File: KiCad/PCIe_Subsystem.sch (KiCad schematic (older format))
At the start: 0 parts

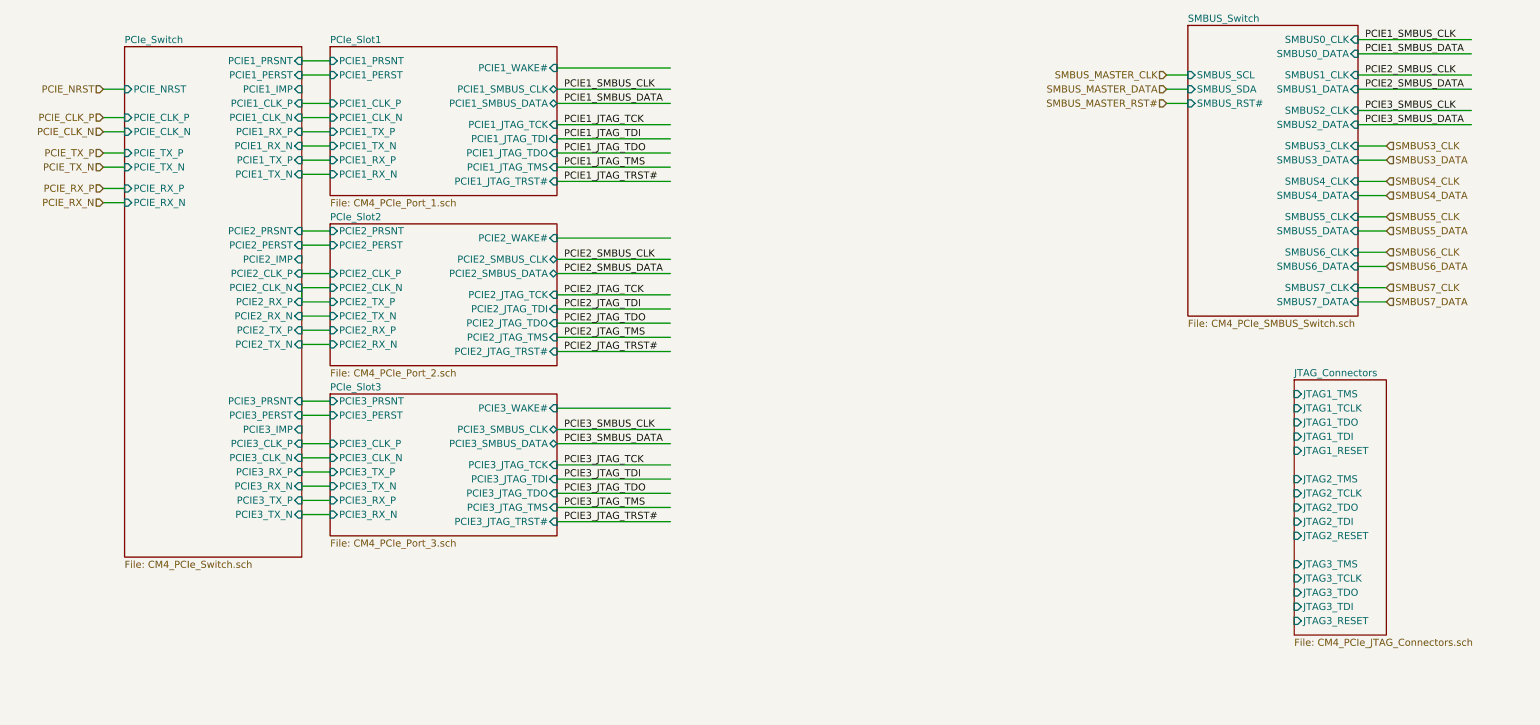
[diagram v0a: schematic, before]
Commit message: Tons of wiring and pin straps for PCI-e Switch
Also re-did some hierarchical labels for JTAG
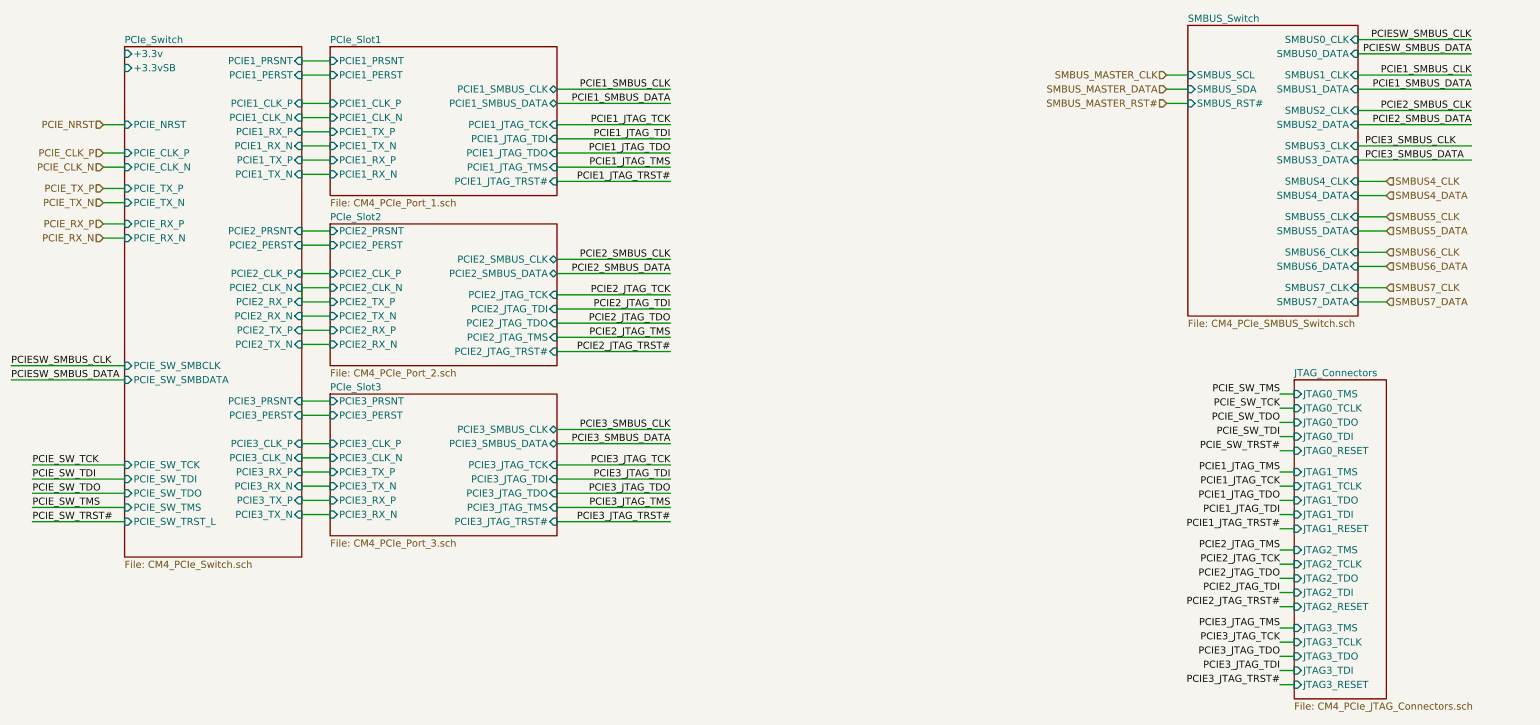
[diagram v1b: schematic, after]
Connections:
- net labels added: PCIESW_SMBUS_CLK, PCIESW_SMBUS_DATA, PCIE_SW_TCK, PCIE_SW_TDI, PCIE_SW_TDO, PCIE_SW_TMS, PCIE_SW_TRST#
- net labels removed: SMBUS3_CLK, SMBUS3_DATA
- wire segments 75 -> 99

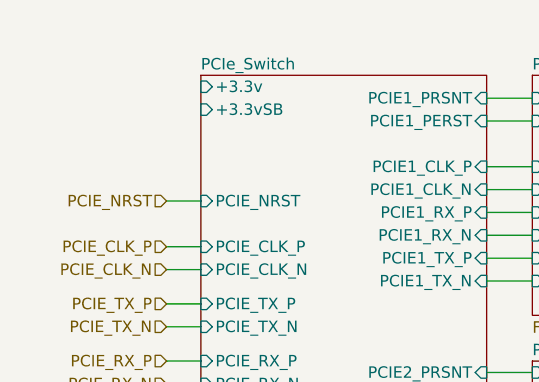
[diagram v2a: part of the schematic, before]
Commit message: PCIe Wiring, resistor value adjustments, and a bunch of small ERC fixes.
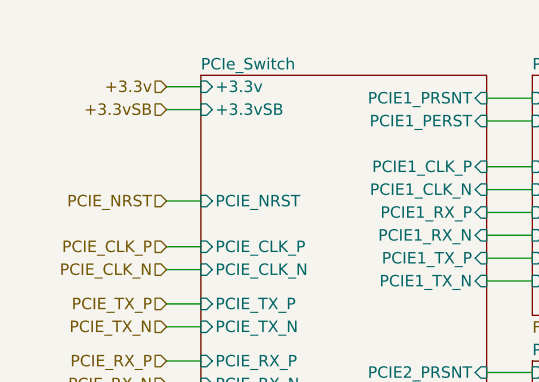
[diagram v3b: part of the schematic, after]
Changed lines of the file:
@@
 Comment4 ""
 $EndDescr
-$Sheet
-S 1300 800  1250 3600
-U 5FFBFEFE
-F0 "PCIe_Switch" 50
-F1 "CM4_PCIe_Switch.sch" 50
-F2 "PCIE_CLK_N" I L 1300 1650 50
-F3 "PCIE_CLK_P" I L 1300 1550 50
-F4 "PCIE_RX_P" I L 1300 2050 50
-F5 "PCIE_RX_N" I L 1300 2150 50
-F6 "PCIE_TX_P" I L 1300 1800 50
-F7 "PCIE_TX_N" I L 1300 1900 50
-F8 "PCIE_NRST" I L 1300 1350 50
-F9 "PCIE1_PRSNT" I R 2550 900 50
-F10 "PCIE2_PRSNT" I R 2550 2100 50
-F11 "PCIE3_PRSNT" I R 2550 3300 50
-F12 "PCIE1_PERST" I R 2550 1000 50
-F13 "PCIE2_PERST" I R 2550 2200 50
-F14 "PCIE3_PERST" I R 2550 3400 50
-F15 "PCIE3_CLK_N" I R 2550 3700 50
-F16 "PCIE3_CLK_P" I R 2550 3600 50
-F17 "PCIE2_CLK_N" I R 2550 2500 50
-F18 "PCIE2_CLK_P" I R 2550 2400 50
-F19 "PCIE1_CLK_N" I R 2550 1300 50
-F20 "PCIE1_CLK_P" I R 2550 1200 50
-F21 "PCIE1_RX_P" I R 2550 1400 50
-F22 "PCIE1_RX_N" I R 2550 1500 50
-F23 "PCIE1_TX_P" I R 2550 1600 50
-F24 "PCIE1_TX_N" I R 2550 1700 50
-F25 "PCIE2_RX_P" I R 2550 2600 50
-F26 "PCIE2_RX_N" I R 2550 2700 50
-F27 "PCIE2_TX_P" I R 2550 2800 50
-F28 "PCIE2_TX_N" I R 2550 2900 50
-F29 "PCIE3_TX_N" I R 2550 4100 50
-F30 "PCIE3_TX_P" I R 2550 4000 50
-F31 "PCIE3_RX_N" I R 2550 3900 50
-F32 "PCIE3_RX_P" I R 2550 3800 50
-F33 "+3.3v" I L 1300 850 50
-F34 "+3.3vSB" I L 1300 950 50
-F35 "PCIE_SW_TDI" I L 1300 3850 50
-F36 "PCIE_SW_TMS" I L 1300 4050 50
-F37 "PCIE_SW_TCK" I L 1300 3750 50
-F38 "PCIE_SW_TDO" I L 1300 3950 50
-F39 "PCIE_SW_TRST_L" I L 1300 4150 50
-F40 "PCIE_SW_SMBCLK" I L 1300 3050 50
-F41 "PCIE_SW_SMBDATA" I L 1300 3150 50
-$EndSheet
 Wire Wire Line
 	2750 4100 2550 4100
@@
 Wire Wire Line
 	2550 900  2750 900
-$Sheet
-S 2750 2050 1600 1000
-U 5FFBFF20
-F0 "PCIe_Slot2" 50
-F1 "CM4_PCIe_Port_2.sch" 50
-F2 "PCIE2_PRSNT" I L 2750 2100 50
-F3 "PCIE2_PERST" I L 2750 2200 50
-F4 "PCIE2_CLK_P" I L 2750 2400 50
-F5 "PCIE2_CLK_N" I L 2750 2500 50
-F6 "PCIE2_RX_P" I L 2750 2800 50
-F7 "PCIE2_RX_N" I L 2750 2900 50
-F8 "PCIE2_TX_N" I L 2750 2700 50
-F9 "PCIE2_TX_P" I L 2750 2600 50
-F10 "PCIE2_SMBUS_CLK" B R 4350 2300 50
-F11 "PCIE2_SMBUS_DATA" B R 4350 2400 50
-F12 "PCIE2_JTAG_TCK" I R 4350 2550 50
-F13 "PCIE2_JTAG_TDI" I R 4350 2650 50
-F14 "PCIE2_JTAG_TDO" I R 4350 2750 50
-F15 "PCIE2_JTAG_TMS" I R 4350 2850 50
-F16 "PCIE2_JTAG_TRST#" I R 4350 2950 50
-$EndSheet
-$Sheet
-S 2750 800  1600 1050
-U 5FFBFF2A
-F0 "PCIe_Slot1" 50
-F1 "CM4_PCIe_Port_1.sch" 50
-F2 "PCIE1_RX_P" I L 2750 1600 50
-F3 "PCIE1_RX_N" I L 2750 1700 50
-F4 "PCIE1_CLK_N" I L 2750 1300 50
-F5 "PCIE1_CLK_P" I L 2750 1200 50
-F6 "PCIE1_PERST" I L 2750 1000 50
-F7 "PCIE1_PRSNT" I L 2750 900 50
-F8 "PCIE1_TX_P" I L 2750 1400 50
-F9 "PCIE1_TX_N" I L 2750 1500 50
-F10 "PCIE1_SMBUS_CLK" B R 4350 1100 50
-F11 "PCIE1_SMBUS_DATA" B R 4350 1200 50
-F12 "PCIE1_JTAG_TCK" I R 4350 1350 50
-F13 "PCIE1_JTAG_TDI" I R 4350 1450 50
-F14 "PCIE1_JTAG_TDO" I R 4350 1550 50
-F15 "PCIE1_JTAG_TMS" I R 4350 1650 50
-F16 "PCIE1_JTAG_TRST#" I R 4350 1750 50
-$EndSheet
-$Sheet
-S 2750 3250 1600 1000
-U 5FFBFF34
-F0 "PCIe_Slot3" 50
-F1 "CM4_PCIe_Port_3.sch" 50
-F2 "PCIE3_PRSNT" I L 2750 3300 50
-F3 "PCIE3_PERST" I L 2750 3400 50
-F4 "PCIE3_CLK_P" I L 2750 3600 50
-F5 "PCIE3_CLK_N" I L 2750 3700 50
-F6 "PCIE3_RX_N" I L 2750 4100 50
-F7 "PCIE3_RX_P" I L 2750 4000 50
-F8 "PCIE3_TX_P" I L 2750 3800 50
-F9 "PCIE3_TX_N" I L 2750 3900 50
-F10 "PCIE3_SMBUS_CLK" B R 4350 3500 50
-F11 "PCIE3_SMBUS_DATA" B R 4350 3600 50
-F12 "PCIE3_JTAG_TCK" I R 4350 3750 50
-F13 "PCIE3_JTAG_TDI" I R 4350 3850 50
-F14 "PCIE3_JTAG_TDO" I R 4350 3950 50
-F15 "PCIE3_JTAG_TMS" I R 4350 4050 50
-F16 "PCIE3_JTAG_TRST#" I R 4350 4150 50
-$EndSheet
 Text HLabel 1150 1350 0    50   Input ~ 0
 PCIE_NRST
@@
 Wire Wire Line
 	10000 850  10800 850
+Text HLabel 1150 850  0    50   Input ~ 0
++3.3v
+Text HLabel 1150 950  0    50   Input ~ 0
++3.3vSB
+Wire Wire Line
+	1150 950  1300 950
+Wire Wire Line
+	1300 850  1150 850
+$Sheet
+S 1300 800  1250 3600
+U 5FFBFEFE
+F0 "PCIe_Switch" 50
+F1 "CM4_PCIe_Switch.sch" 50
+F2 "PCIE_CLK_N" I L 1300 1650 50
+F3 "PCIE_CLK_P" I L 1300 1550 50
+F4 "PCIE_RX_P" I L 1300 2050 50
+F5 "PCIE_RX_N" I L 1300 2150 50
+F6 "PCIE_TX_P" I L 1300 1800 50
+F7 "PCIE_TX_N" I L 1300 1900 50
+F8 "PCIE_NRST" I L 1300 1350 50
+F9 "PCIE1_PRSNT" I R 2550 900 50
+F10 "PCIE2_PRSNT" I R 2550 2100 50
+F11 "PCIE3_PRSNT" I R 2550 3300 50
+F12 "PCIE1_PERST" I R 2550 1000 50
+F13 "PCIE2_PERST" I R 2550 2200 50
+F14 "PCIE3_PERST" I R 2550 3400 50
+F15 "PCIE3_CLK_N" I R 2550 3700 50
+F16 "PCIE3_CLK_P" I R 2550 3600 50
+F17 "PCIE2_CLK_N" I R 2550 2500 50
+F18 "PCIE2_CLK_P" I R 2550 2400 50
+F19 "PCIE1_CLK_N" I R 2550 1300 50
+F20 "PCIE1_CLK_P" I R 2550 1200 50
+F21 "PCIE1_RX_P" I R 2550 1400 50
+F22 "PCIE1_RX_N" I R 2550 1500 50
+F23 "PCIE1_TX_P" I R 2550 1600 50
+F24 "PCIE1_TX_N" I R 2550 1700 50
+F25 "PCIE2_RX_P" I R 2550 2600 50
+F26 "PCIE2_RX_N" I R 2550 2700 50
+F27 "PCIE2_TX_P" I R 2550 2800 50
+F28 "PCIE2_TX_N" I R 2550 2900 50
+F29 "PCIE3_TX_N" I R 2550 4100 50
+F30 "PCIE3_TX_P" I R 2550 4000 50
+F31 "PCIE3_RX_N" I R 2550 3900 50
+F32 "PCIE3_RX_P" I R 2550 3800 50
+F33 "+3.3v" I L 1300 850 50
+F34 "+3.3vSB" I L 1300 950 50
+F35 "PCIE_SW_TDI" I L 1300 3850 50
+F36 "PCIE_SW_TMS" I L 1300 4050 50
+F37 "PCIE_SW_TCK" I L 1300 3750 50
+F38 "PCIE_SW_TDO" I L 1300 3950 50
+F39 "PCIE_SW_TRST_L" I L 1300 4150 50
+F40 "PCIE_SW_SMBCLK" I L 1300 3050 50
+F41 "PCIE_SW_SMBDATA" I L 1300 3150 50
+$EndSheet
+$Sheet
+S 2750 3250 1600 1000
+U 5FFBFF34
+F0 "PCIe_Slot3" 50
+F1 "CM4_PCIe_Port_3.sch" 50
+F2 "PCIE3_PRSNT" I L 2750 3300 50
+F3 "PCIE3_PERST" I L 2750 3400 50
+F4 "PCIE3_CLK_P" I L 2750 3600 50
+F5 "PCIE3_CLK_N" I L 2750 3700 50
+F6 "PCIE3_RX_N" I L 2750 4100 50
+F7 "PCIE3_RX_P" I L 2750 4000 50
+F8 "PCIE3_TX_P" I L 2750 3800 50
+F9 "PCIE3_TX_N" I L 2750 3900 50
+F10 "PCIE3_SMBUS_CLK" B R 4350 3500 50
+F11 "PCIE3_SMBUS_DATA" B R 4350 3600 50
+F12 "PCIE3_JTAG_TCK" I R 4350 3750 50
+F13 "PCIE3_JTAG_TDI" I R 4350 3850 50
+F14 "PCIE3_JTAG_TDO" I R 4350 3950 50
+F15 "PCIE3_JTAG_TMS" I R 4350 4050 50
+F16 "PCIE3_JTAG_TRST#" I R 4350 4150 50
+$EndSheet
+$Sheet
+S 2750 800  1600 1050
+U 5FFBFF2A
+F0 "PCIe_Slot1" 50
+F1 "CM4_PCIe_Port_1.sch" 50
+F2 "PCIE1_RX_P" I L 2750 1600 50
+F3 "PCIE1_RX_N" I L 2750 1700 50
+F4 "PCIE1_CLK_N" I L 2750 1300 50
+F5 "PCIE1_CLK_P" I L 2750 1200 50
+F6 "PCIE1_PERST" I L 2750 1000 50
+F7 "PCIE1_PRSNT" I L 2750 900 50
+F8 "PCIE1_TX_P" I L 2750 1400 50
+F9 "PCIE1_TX_N" I L 2750 1500 50
+F10 "PCIE1_SMBUS_CLK" B R 4350 1100 50
+F11 "PCIE1_SMBUS_DATA" B R 4350 1200 50
+F12 "PCIE1_JTAG_TCK" I R 4350 1350 50
+F13 "PCIE1_JTAG_TDI" I R 4350 1450 50
+F14 "PCIE1_JTAG_TDO" I R 4350 1550 50
+F15 "PCIE1_JTAG_TMS" I R 4350 1650 50
+F16 "PCIE1_JTAG_TRST#" I R 4350 1750 50
+$EndSheet
+$Sheet
+S 2750 2050 1600 1000
+U 5FFBFF20
+F0 "PCIe_Slot2" 50
+F1 "CM4_PCIe_Port_2.sch" 50
+F2 "PCIE2_PRSNT" I L 2750 2100 50
+F3 "PCIE2_PERST" I L 2750 2200 50
+F4 "PCIE2_CLK_P" I L 2750 2400 50
+F5 "PCIE2_CLK_N" I L 2750 2500 50
+F6 "PCIE2_RX_P" I L 2750 2800 50
+F7 "PCIE2_RX_N" I L 2750 2900 50
+F8 "PCIE2_TX_N" I L 2750 2700 50
+F9 "PCIE2_TX_P" I L 2750 2600 50
+F10 "PCIE2_SMBUS_CLK" B R 4350 2300 50
+F11 "PCIE2_SMBUS_DATA" B R 4350 2400 50
+F12 "PCIE2_JTAG_TCK" I R 4350 2550 50
+F13 "PCIE2_JTAG_TDI" I R 4350 2650 50
+F14 "PCIE2_JTAG_TDO" I R 4350 2750 50
+F15 "PCIE2_JTAG_TMS" I R 4350 2850 50
+F16 "PCIE2_JTAG_TRST#" I R 4350 2950 50
+$EndSheet
 $EndSCHEMATC

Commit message: Imported new components to the PCB and moved some components
Updated PDFs and added two new board layers. One for ground and a second for power (voltage to be decided)
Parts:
- added J8: Conn_02x05_Odd_Even, CM4_MATX:PinHeader_2x05_P2.54mm_Vertical, symbol CM4_MATX:Conn_02x05_Odd_Even
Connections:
- net labels added: +3.3VP, GND, PCIE_SW_TRST_L
- net labels removed: PCIE1_JTAG_TCK, PCIE1_JTAG_TDI, PCIE1_JTAG_TDO, PCIE1_JTAG_TMS, PCIE1_JTAG_TRST#, PCIE2_JTAG_TCK, PCIE2_JTAG_TDI, PCIE2_JTAG_TDO, PCIE2_JTAG_TMS, PCIE2_JTAG_TRST#, PCIE3_JTAG_TCK, PCIE3_JTAG_TDI, PCIE3_JTAG_TDO, PCIE3_JTAG_TMS, PCIE3_JTAG_TRST#
- wire segments 101 -> 81
- no-connect marks 0 -> 1
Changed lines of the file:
@@
 $Descr A4 11693 8268
 encoding utf-8
-Sheet 10 16
+Sheet 10 15
 Title ""
 Date "2021-02-08"
@@
 Wire Wire Line
 	2550 2900 2750 2900
-Wire Wire Line
-	4350 1350 5150 1350
-Wire Wire Line
-	4350 1450 5150 1450
-Wire Wire Line
-	4350 1550 5150 1550
-Wire Wire Line
-	4350 1650 5150 1650
-Wire Wire Line
-	4350 1750 5150 1750
-Wire Wire Line
-	4350 2550 5150 2550
-Wire Wire Line
-	4350 2650 5150 2650
-Wire Wire Line
-	4350 2750 5150 2750
-Wire Wire Line
-	4350 2850 5150 2850
-Wire Wire Line
-	4350 2950 5150 2950
-Wire Wire Line
-	4350 3750 5150 3750
-Wire Wire Line
-	4350 3850 5150 3850
-Wire Wire Line
-	4350 3950 5150 3950
-Wire Wire Line
-	4350 4050 5150 4050
-Wire Wire Line
-	4350 4150 5150 4150
-$Sheet
-S 9550 3150 650  2250
-U 60261DAF
-F0 "JTAG_Connectors" 50
-F1 "CM4_PCIe_JTAG_Connectors.sch" 50
-F2 "JTAG1_TMS" I L 9550 3800 50
-F3 "JTAG1_TCLK" I L 9550 3900 50
-F4 "JTAG1_TDO" I L 9550 4000 50
-F5 "JTAG1_TDI" I L 9550 4100 50
-F6 "JTAG1_RESET" I L 9550 4200 50
-F7 "JTAG2_TMS" I L 9550 4350 50
-F8 "JTAG2_TCLK" I L 9550 4450 50
-F9 "JTAG2_TDO" I L 9550 4550 50
-F10 "JTAG2_TDI" I L 9550 4650 50
-F11 "JTAG2_RESET" I L 9550 4750 50
-F12 "JTAG3_TMS" I L 9550 4900 50
-F13 "JTAG3_TCLK" I L 9550 5000 50
-F14 "JTAG3_TDO" I L 9550 5100 50
-F15 "JTAG3_TDI" I L 9550 5200 50
-F16 "JTAG3_RESET" I L 9550 5300 50
-F17 "JTAG0_TMS" I L 9550 3250 50
-F18 "JTAG0_TCLK" I L 9550 3350 50
-F19 "JTAG0_TDO" I L 9550 3450 50
-F20 "JTAG0_TDI" I L 9550 3550 50
-F21 "JTAG0_RESET" I L 9550 3650 50
-$EndSheet
-Text Label 5150 1350 2    50   ~ 0
-PCIE1_JTAG_TCK
-Text Label 5150 1450 2    50   ~ 0
-PCIE1_JTAG_TDI
-Text Label 5150 1550 2    50   ~ 0
-PCIE1_JTAG_TDO
-Text Label 5150 1650 2    50   ~ 0
-PCIE1_JTAG_TMS
-Text Label 5150 1750 2    50   ~ 0
-PCIE1_JTAG_TRST#
-Text Label 5150 2550 2    50   ~ 0
-PCIE2_JTAG_TCK
-Text Label 5150 2650 2    50   ~ 0
-PCIE2_JTAG_TDI
-Text Label 5150 2750 2    50   ~ 0
-PCIE2_JTAG_TDO
-Text Label 5150 2850 2    50   ~ 0
-PCIE2_JTAG_TMS
-Text Label 5150 2950 2    50   ~ 0
-PCIE2_JTAG_TRST#
-Text Label 5150 3750 2    50   ~ 0
-PCIE3_JTAG_TCK
-Text Label 5150 3850 2    50   ~ 0
-PCIE3_JTAG_TDI
-Text Label 5150 3950 2    50   ~ 0
-PCIE3_JTAG_TDO
-Text Label 5150 4050 2    50   ~ 0
-PCIE3_JTAG_TMS
-Text Label 5150 4150 2    50   ~ 0
-PCIE3_JTAG_TRST#
 Text Label 650  3750 0    50   ~ 0
 PCIE_SW_TCK
@@
 Wire Wire Line
 	650  4150 1300 4150
-Text Label 9450 5000 2    50   ~ 0
-PCIE3_JTAG_TCK
-Text Label 9450 5200 2    50   ~ 0
-PCIE3_JTAG_TDI
-Text Label 9450 5100 2    50   ~ 0
-PCIE3_JTAG_TDO
-Text Label 9450 5300 2    50   ~ 0
-PCIE3_JTAG_TRST#
-Text Label 9450 4900 2    50   ~ 0
-PCIE3_JTAG_TMS
-Text Label 9450 4750 2    50   ~ 0
-PCIE2_JTAG_TRST#
-Text Label 9450 4350 2    50   ~ 0
-PCIE2_JTAG_TMS
-Text Label 9450 3900 2    50   ~ 0
-PCIE1_JTAG_TCK
-Text Label 9450 4100 2    50   ~ 0
-PCIE1_JTAG_TDI
-Text Label 9450 4200 2    50   ~ 0
-PCIE1_JTAG_TRST#
-Text Label 9450 3800 2    50   ~ 0
-PCIE1_JTAG_TMS
-Text Label 9450 4000 2    50   ~ 0
-PCIE1_JTAG_TDO
-Text Label 9450 4650 2    50   ~ 0
-PCIE2_JTAG_TDI
-Text Label 9450 4550 2    50   ~ 0
-PCIE2_JTAG_TDO
-Text Label 9450 4450 2    50   ~ 0
-PCIE2_JTAG_TCK
-Text Label 9450 3350 2    50   ~ 0
-PCIE_SW_TCK
-Text Label 9450 3550 2    50   ~ 0
-PCIE_SW_TDI
-Text Label 9450 3450 2    50   ~ 0
-PCIE_SW_TDO
-Text Label 9450 3650 2    50   ~ 0
-PCIE_SW_TRST#
-Text Label 9450 3250 2    50   ~ 0
-PCIE_SW_TMS
-Wire Wire Line
-	9450 3250 9550 3250
-Wire Wire Line
-	9450 3450 9550 3450
-Wire Wire Line
-	9450 3550 9550 3550
-Wire Wire Line
-	9450 3650 9550 3650
-Wire Wire Line
-	9550 3800 9450 3800
-Wire Wire Line
-	9450 3900 9550 3900
-Wire Wire Line
-	9550 4000 9450 4000
-Wire Wire Line
-	9450 4100 9550 4100
-Wire Wire Line
-	9550 4200 9450 4200
-Wire Wire Line
-	9450 4350 9550 4350
-Wire Wire Line
-	9450 4450 9550 4450
-Wire Wire Line
-	9450 4550 9550 4550
-Wire Wire Line
-	9450 4650 9550 4650
-Wire Wire Line
-	9450 4750 9550 4750
-Wire Wire Line
-	9450 4900 9550 4900
-Wire Wire Line
-	9450 5000 9550 5000
-Wire Wire Line
-	9450 5100 9550 5100
-Wire Wire Line
-	9450 5200 9550 5200
-Wire Wire Line
-	9450 5300 9550 5300
-Wire Wire Line
-	9450 3350 9550 3350
 Wire Wire Line
 	10000 1600 10800 1600
@@
 F10 "PCIE3_SMBUS_CLK" B R 4350 3500 50
 F11 "PCIE3_SMBUS_DATA" B R 4350 3600 50
-F12 "PCIE3_JTAG_TCK" I R 4350 3750 50
-F13 "PCIE3_JTAG_TDI" I R 4350 3850 50
-F14 "PCIE3_JTAG_TDO" I R 4350 3950 50
-F15 "PCIE3_JTAG_TMS" I R 4350 4050 50
-F16 "PCIE3_JTAG_TRST#" I R 4350 4150 50
 $EndSheet
 $Sheet
@@
 F10 "PCIE1_SMBUS_CLK" B R 4350 1100 50
 F11 "PCIE1_SMBUS_DATA" B R 4350 1200 50
-F12 "PCIE1_JTAG_TCK" I R 4350 1350 50
-F13 "PCIE1_JTAG_TDI" I R 4350 1450 50
-F14 "PCIE1_JTAG_TDO" I R 4350 1550 50
-F15 "PCIE1_JTAG_TMS" I R 4350 1650 50
-F16 "PCIE1_JTAG_TRST#" I R 4350 1750 50
 $EndSheet
+$Comp
+L CM4_MATX:Conn_02x05_Odd_Even J?
+U 1 1 6095C986
+P 9450 4850
+AR Path="/5FFBC089/60261DAF/6095C986" Ref="J?"  Part="1"
+AR Path="/5FFBC089/6095C986" Ref="J8"  Part="1"
+F 0 "J8" H 9500 5267 50  0000 C CNN
+F 1 "Conn_02x05_Odd_Even" H 9500 5176 50  0000 C CNN
+F 2 "CM4_MATX:PinHeader_2x05_P2.54mm_Vertical" H 9450 4850 50  0001 C CNN
+F 3 "~" H 9450 4850 50  0001 C CNN
+F 4 "Standard 2.54mm (100mil)-separated pins" H 9450 4850 50  0001 C CNN "Description"
+	1    9450 4850
+	1    0    0    -1
+$EndComp
+Wire Wire Line
+	9750 4950 9950 4950
+$Comp
+L CM4_MATX:+3.3VP #PWR?
+U 1 1 6095C996
+P 9000 4450
+AR Path="/5FFBC089/60261DAF/6095C996" Ref="#PWR?"  Part="1"
+AR Path="/5FFBC089/6095C996" Ref="#PWR03"  Part="1"
+F 0 "#PWR03" H 9150 4400 50  0001 C CNN
+F 1 "+3.3VP" H 9015 4623 50  0000 C CNN
+F 2 "" H 9000 4450 50  0001 C CNN
+F 3 "" H 9000 4450 50  0001 C CNN
+	1    9000 4450
+	1    0    0    -1
+$EndComp
+Wire Wire Line
+	9000 4450 9000 4650
+Wire Wire Line
+	9000 4650 9250 4650
+Wire Wire Line
+	9000 4750 9250 4750
+$Comp
+L CM4_MATX:GND #PWR?
+U 1 1 6095C99F
+P 9000 5150
+AR Path="/5FFBC089/60261DAF/6095C99F" Ref="#PWR?"  Part="1"
+AR Path="/5FFBC089/6095C99F" Ref="#PWR04"  Part="1"
+F 0 "#PWR04" H 9000 4900 50  0001 C CNN
+F 1 "GND" H 9005 4977 50  0000 C CNN
+F 2 "" H 9000 5150 50  0001 C CNN
+F 3 "" H 9000 5150 50  0001 C CNN
+	1    9000 5150
+	1    0    0    -1
+$EndComp
+Wire Wire Line
+	9000 5150 9000 5050
+Wire Wire Line
+	9000 5050 9250 5050
+Wire Wire Line
+	9000 5050 9000 4850
+Connection ~ 9000 5050
+Wire Wire Line
+	9250 4850 9000 4850
+Connection ~ 9000 4850
+Wire Wire Line
+	9000 4850 9000 4750
+Wire Wire Line
+	9250 4950 9050 4950
+NoConn ~ 9050 4950
 $Sheet
 S 2750 2050 1600 1000
@@
 F10 "PCIE2_SMBUS_CLK" B R 4350 2300 50
 F11 "PCIE2_SMBUS_DATA" B R 4350 2400 50
-F12 "PCIE2_JTAG_TCK" I R 4350 2550 50
-F13 "PCIE2_JTAG_TDI" I R 4350 2650 50
-F14 "PCIE2_JTAG_TDO" I R 4350 2750 50
-F15 "PCIE2_JTAG_TMS" I R 4350 2850 50
-F16 "PCIE2_JTAG_TRST#" I R 4350 2950 50
 $EndSheet
+Text Label 10450 4650 2    50   ~ 0
+PCIE_SW_TMS
+Text Label 10450 4750 2    50   ~ 0
+PCIE_SW_TCK
+Text Label 10450 4850 2    50   ~ 0
+PCIE_SW_TDO
+Text Label 10450 4950 2    50   ~ 0
+PCIE_SW_TDI
+Text Label 10450 5050 2    50   ~ 0
+PCIE_SW_TRST_L
+Wire Wire Line
+	9750 4650 10450 4650
+Wire Wire Line
+	9750 4750 10450 4750
+Wire Wire Line
+	9750 4850 10400 4850
+Wire Wire Line
+	10000 4950 10450 4950
+Wire Wire Line
+	9750 5050 10400 5050
 $EndSCHEMATC

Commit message: Connected all grounds in the schematic and planes
Planes:
In 1 - Ground
In 2 - 3.3v Zone which excludes the IO and 5v Zone around only the IO
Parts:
- added GND: GND, symbol CM4_MATX:GND
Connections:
- net labels removed: GND
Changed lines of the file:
@@
 P 9000 5150
 AR Path="/5FFBC089/60261DAF/6095C99F" Ref="#PWR?"  Part="1"
-AR Path="/5FFBC089/6095C99F" Ref="#PWR04"  Part="1"
-F 0 "#PWR04" H 9000 4900 50  0001 C CNN
+AR Path="/5FFBC089/6095C99F" Ref="GND"  Part="1"
+F 0 "GND" H 9000 4900 50  0001 C CNN
 F 1 "GND" H 9005 4977 50  0000 C CNN
 F 2 "" H 9000 5150 50  0001 C CNN
